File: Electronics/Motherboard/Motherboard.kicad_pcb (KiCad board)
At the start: 4 copper layers, 113.4 x 56 mm, 53 parts, among them J1 DX07S024JJ3R1300, M1 AO3400A, M2 AO3400A, M3 AO3400A, U1 AMS1117-3.3, U2 TMC2209_SILENTSTEPSTICK, U3 TMC2209_SILENTSTEPSTICK, U4 TMC2209_SILENTSTEPSTICK, U5 TMC2209_SILENTSTEPSTICK, U6 LM2576HVS-5

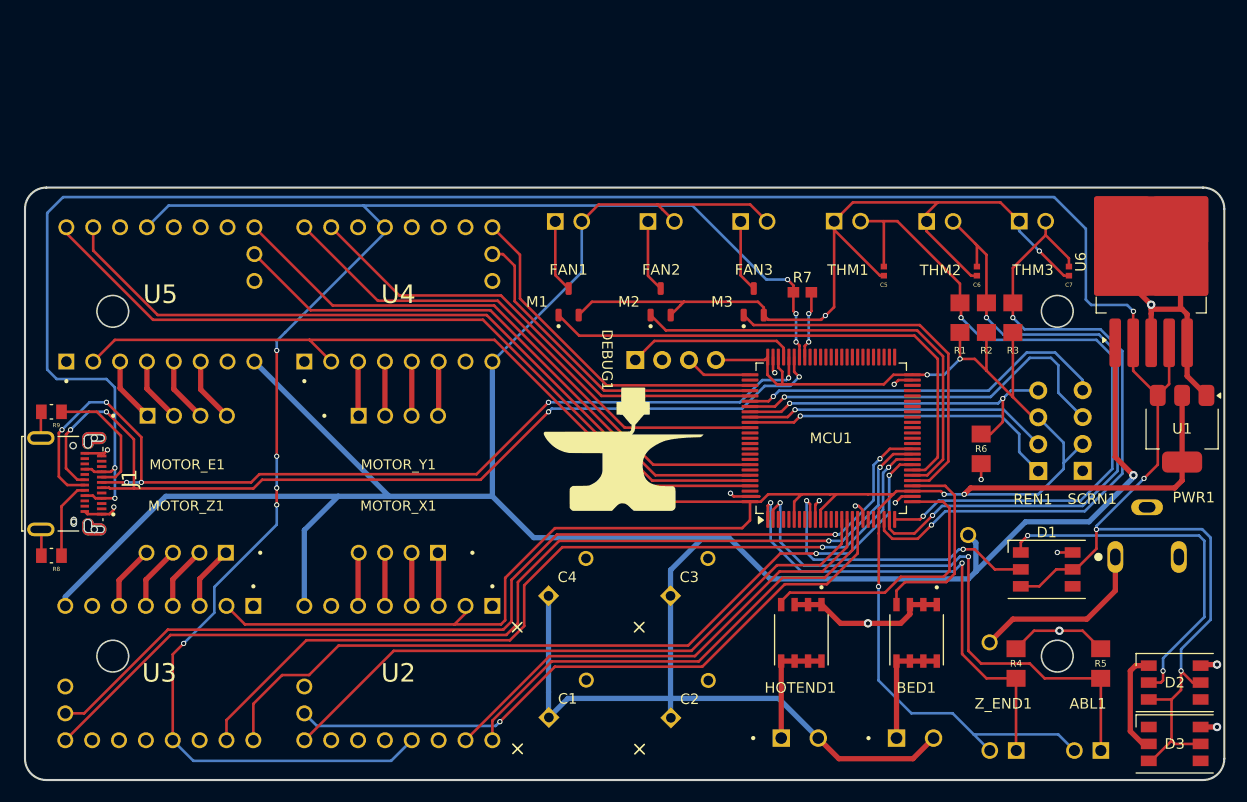
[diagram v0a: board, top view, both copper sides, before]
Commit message: added capacitors and JST connector (except 331 because i don't have CAD)
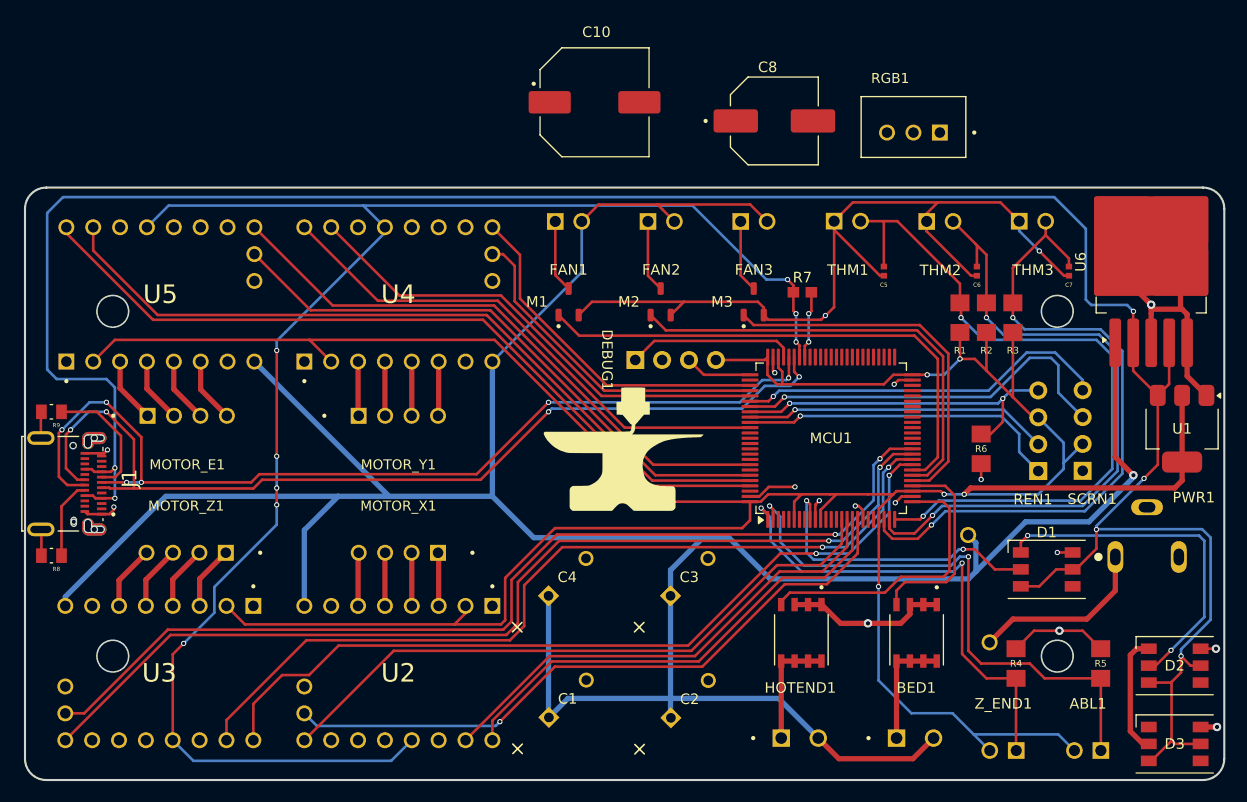
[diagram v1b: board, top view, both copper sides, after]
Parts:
- added C10: UWT1V221MNL1GS, UWT1V221MNL1GS:CAPAE1030X1080N_UWT1H221MNL1GS, F.Cu at (154.2, 63.9)
- added C8: UWT1V101MCL1GS, UWT1V101MCL1GS:CAPAE830X1000N, F.Cu at (171.2, 65.7)
- added RGB1: B3B-XH-A, B3B-XH-A:JST_B3B-XH-A_LF__SN_, F.Cu at (184.4, 66.3)
- moved D2 1.60 mm to (209.1, 117.2)
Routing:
- net Net-(D1-DOUT): track 35.0 -> 33.1 mm
- net Net-(D2-DOUT): track 9.90 -> 11.4 mm
- net GNDREF: track 157.6 -> 158.5 mm
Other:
- board text added: "PCB by @awdev and @blaze"
